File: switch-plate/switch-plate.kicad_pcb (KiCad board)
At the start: 2 copper layers, 113.8 x 96.9 mm, 23 parts, among them SW1 SW_Push, SW10 SW_Push, SW11 SW_Push, SW12 SW_Push, SW13 SW_Push, SW14 SW_Push, SW15 SW_Push, SW16 SW_Push, SW17 SW_Push, SW18 SW_Push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

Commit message: tt
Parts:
- G***: footprint project:gears -> switch-plate:gears
- SW1, SW10, SW11, SW12, SW13, SW14, SW15, SW16, SW17, SW18, SW2, SW3, SW4, SW5, SW6, SW7, SW8, SW9: footprint project:Switch_Cut -> switch-plate:Switch_Cut

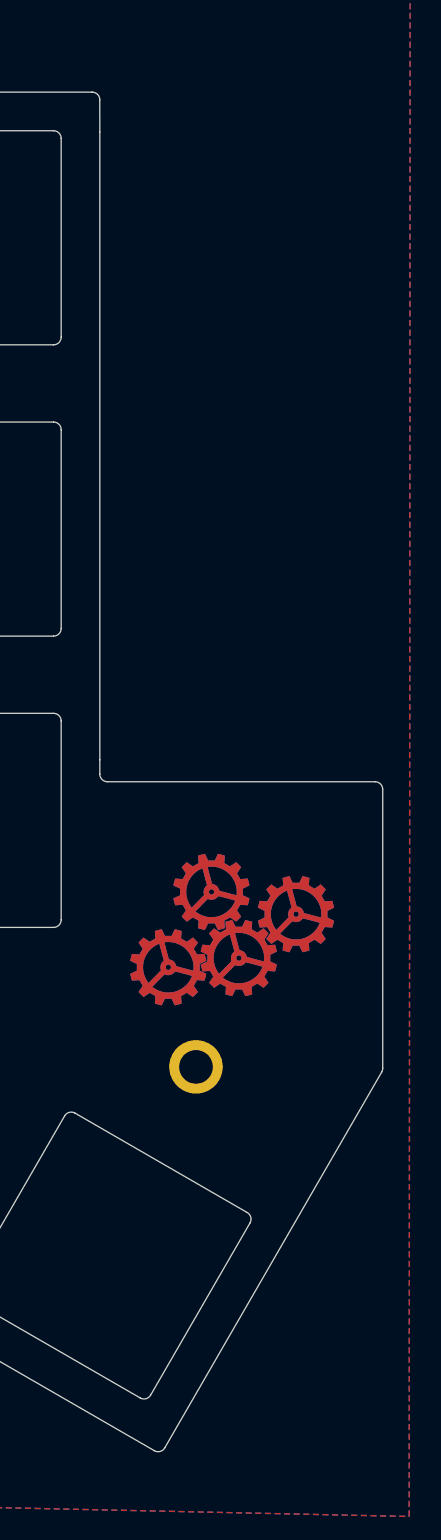
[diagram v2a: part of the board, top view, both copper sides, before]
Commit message: In the process of transitioning the board to use the SEEED XIAO instead of a pro micro
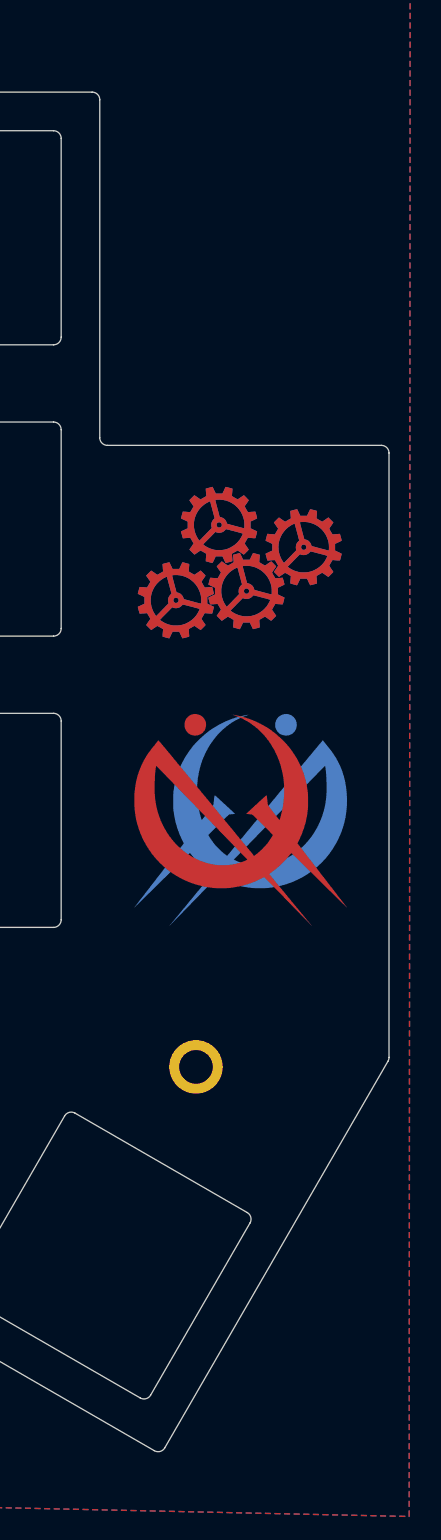
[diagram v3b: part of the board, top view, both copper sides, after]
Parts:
- added G***: LOGO, switch-plate:copper, F.Cu at (189.5, 104.5)
- moved G*** 24.0 mm to (189.5, 87.5)
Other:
- board size 113.8 x 96.9 mm -> 114.2 x 96.9 mm
